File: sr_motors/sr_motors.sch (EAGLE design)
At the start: 20 parts

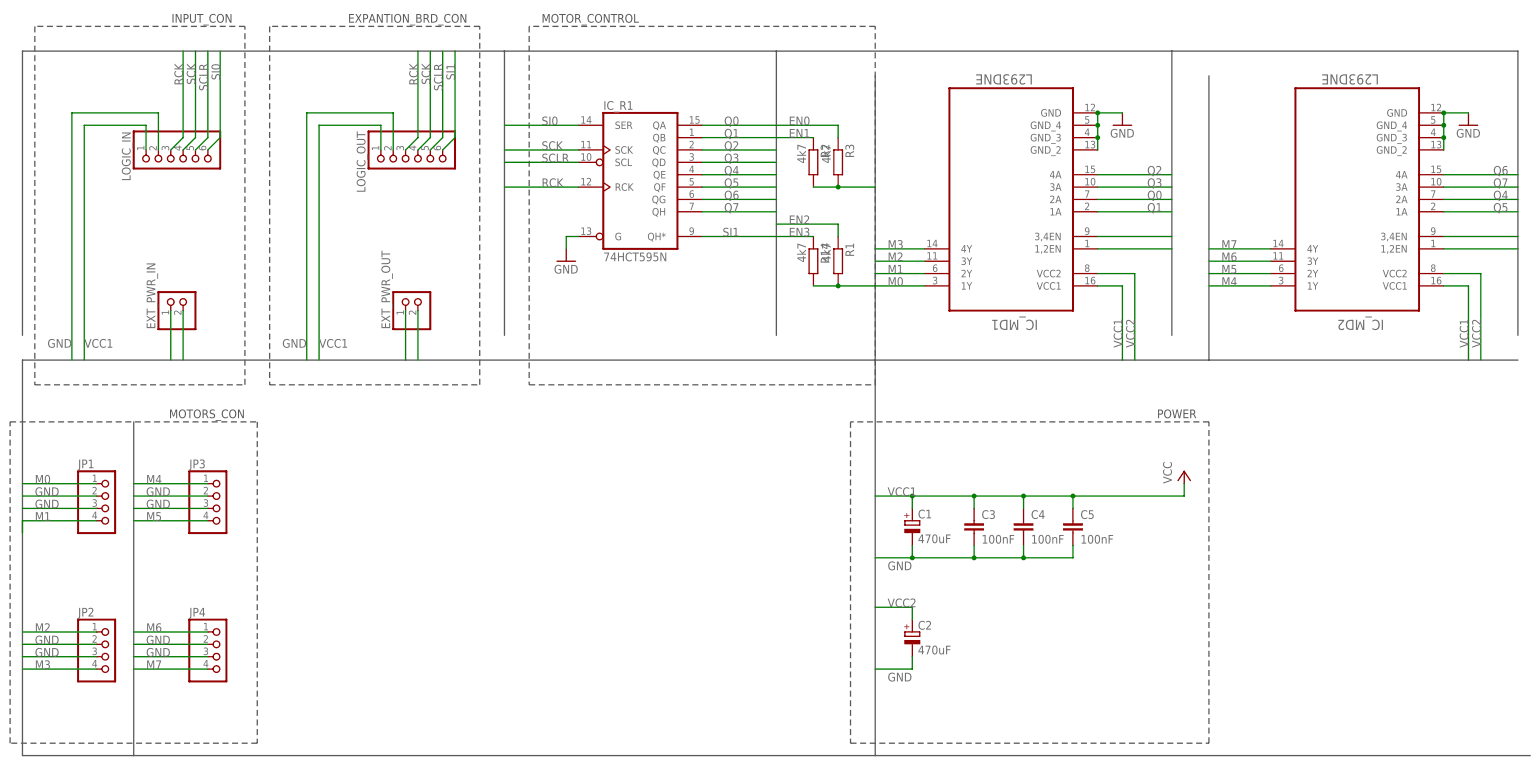
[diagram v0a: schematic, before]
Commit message: Verion 1.2: Increased route width and board width, small other changes
Squashed commit of the following:

commit cb5b4ae53fc73325e271569d8207a4f4cb0d995e
Author: Sergey Kostyuk <contact@s-kostyuk.me>
Date:   Tue Sep 13 19:34:33 2016 +0300

    Increaded width of routes, increased board width, replaced capacitor package, updated board version

commit 30ef558f6f82cadcaf764826f9decc7df1a17ce0
Author: Sergey Kostyuk <contact@s-kostyuk.me>
Date:   Tue Sep 13 19:27:19 2016 +0300

    Replaced capacitor package

commit a2d398c50457a8d09da237926f830a1984b8064b
Author: Sergey Kostyuk <contact@s-kostyuk.me>
Date:   Tue Sep 13 18:08:38 2016 +0300

    Icreased width of routes, icreased board width

commit f5951c6459f5b93fe179c3fabd85f49e6b5260dd
Author: Sergey Kostyuk <contact@s-kostyuk.me>
Date:   Wed Sep 7 16:51:49 2016 +0300

    Increased width of power lines on sr_motors

commit 1e2f38b3539c2f4abccb8c8183ef937e4e63213c
Author: Sergey Kostyuk <ks.hot.ua@gmail.com>
Date:   Mon Aug 22 15:17:33 2016 +0300

    Added reverse current protection for external power, added version text
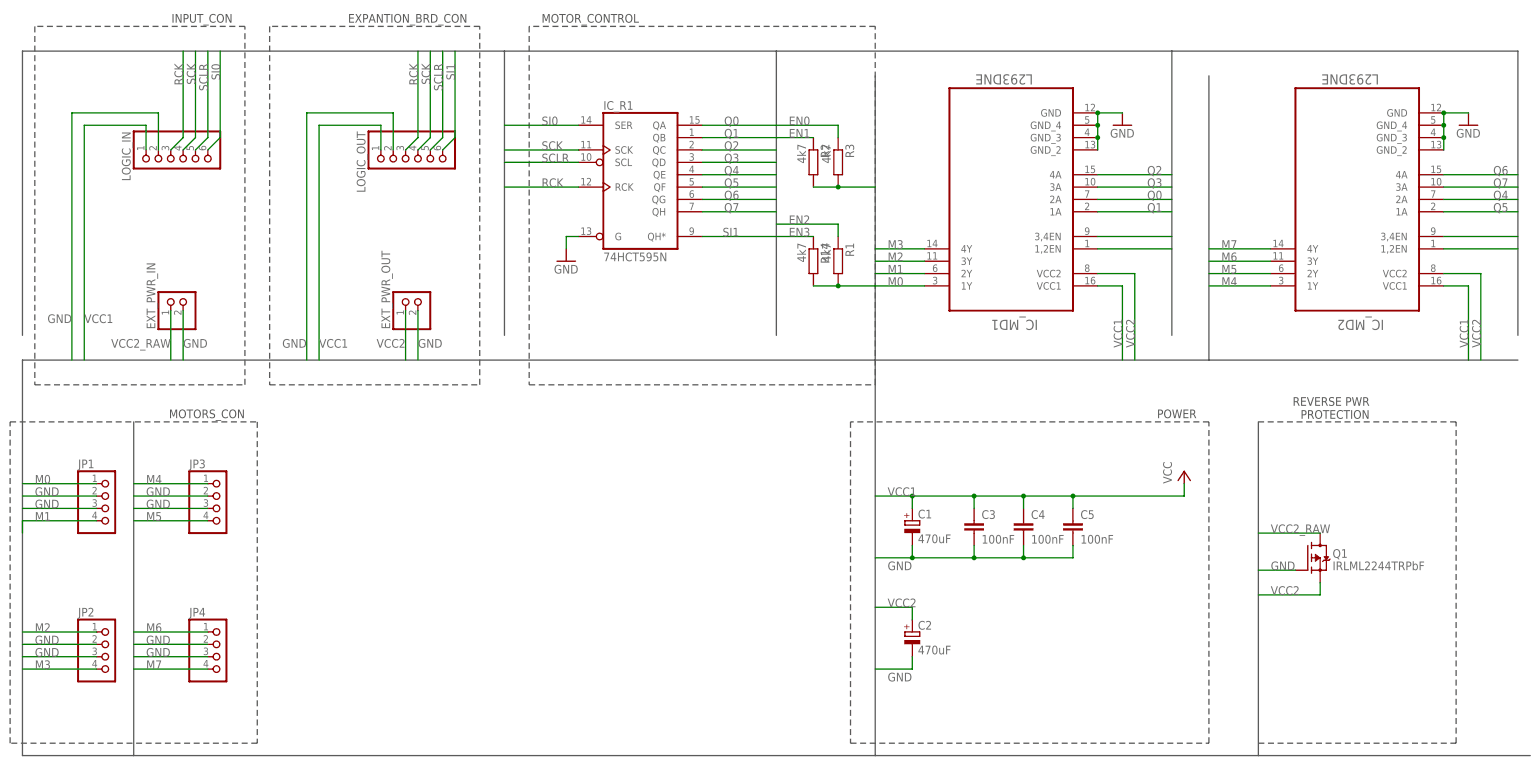
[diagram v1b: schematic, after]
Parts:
- added Q1: IRLML2244TRPbF, we-transistor:MOSFET-P-SOT23
- C1, C2: device rcl:CPOL-EUTAP5-60 -> rcl:CPOL-EUTT2D6
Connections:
- new net VCC2_RAW: EXT_PWR_IN.1, Q1.D
- net GND: now also Q1.G
- net VCC2: now also Q1.S; no longer EXT_PWR_IN.1
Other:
- note added: "REVERSE PWR PROTECTION"
